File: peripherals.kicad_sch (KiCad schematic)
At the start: 15 parts, among them U5 LSM6DSO, U6 W25Q128JVS, U7 LIS3MDL

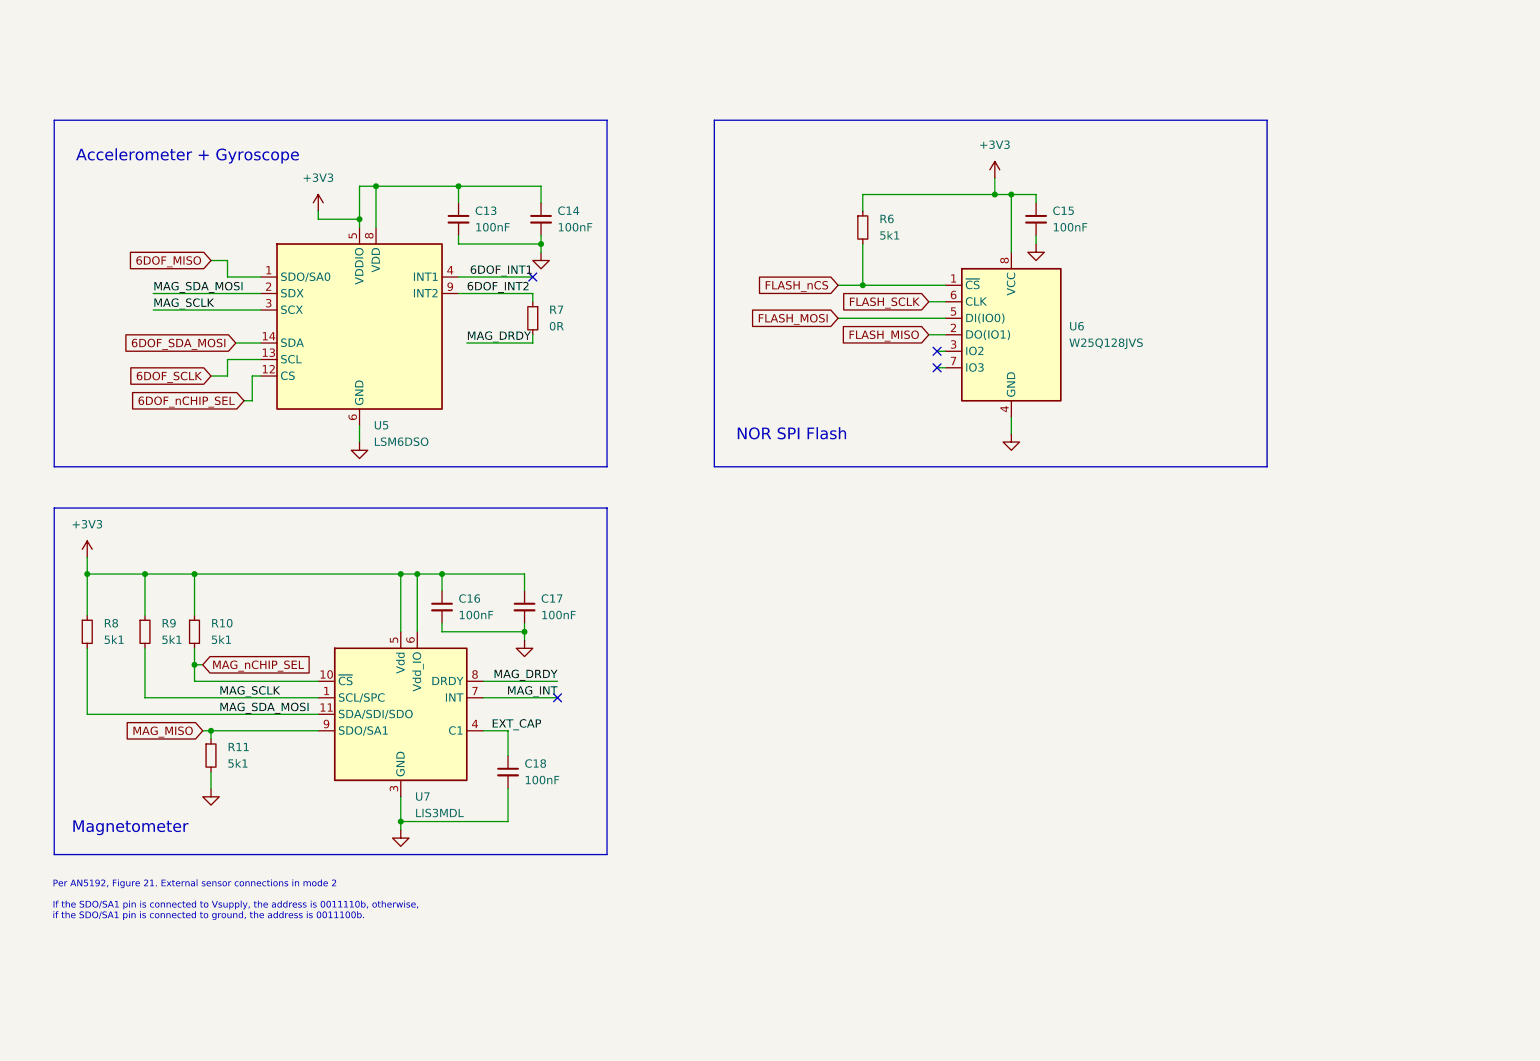
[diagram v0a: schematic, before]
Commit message: Added an I2C IO expander, plus 2 pushbuttons and  2 LEDs controlled by the expander
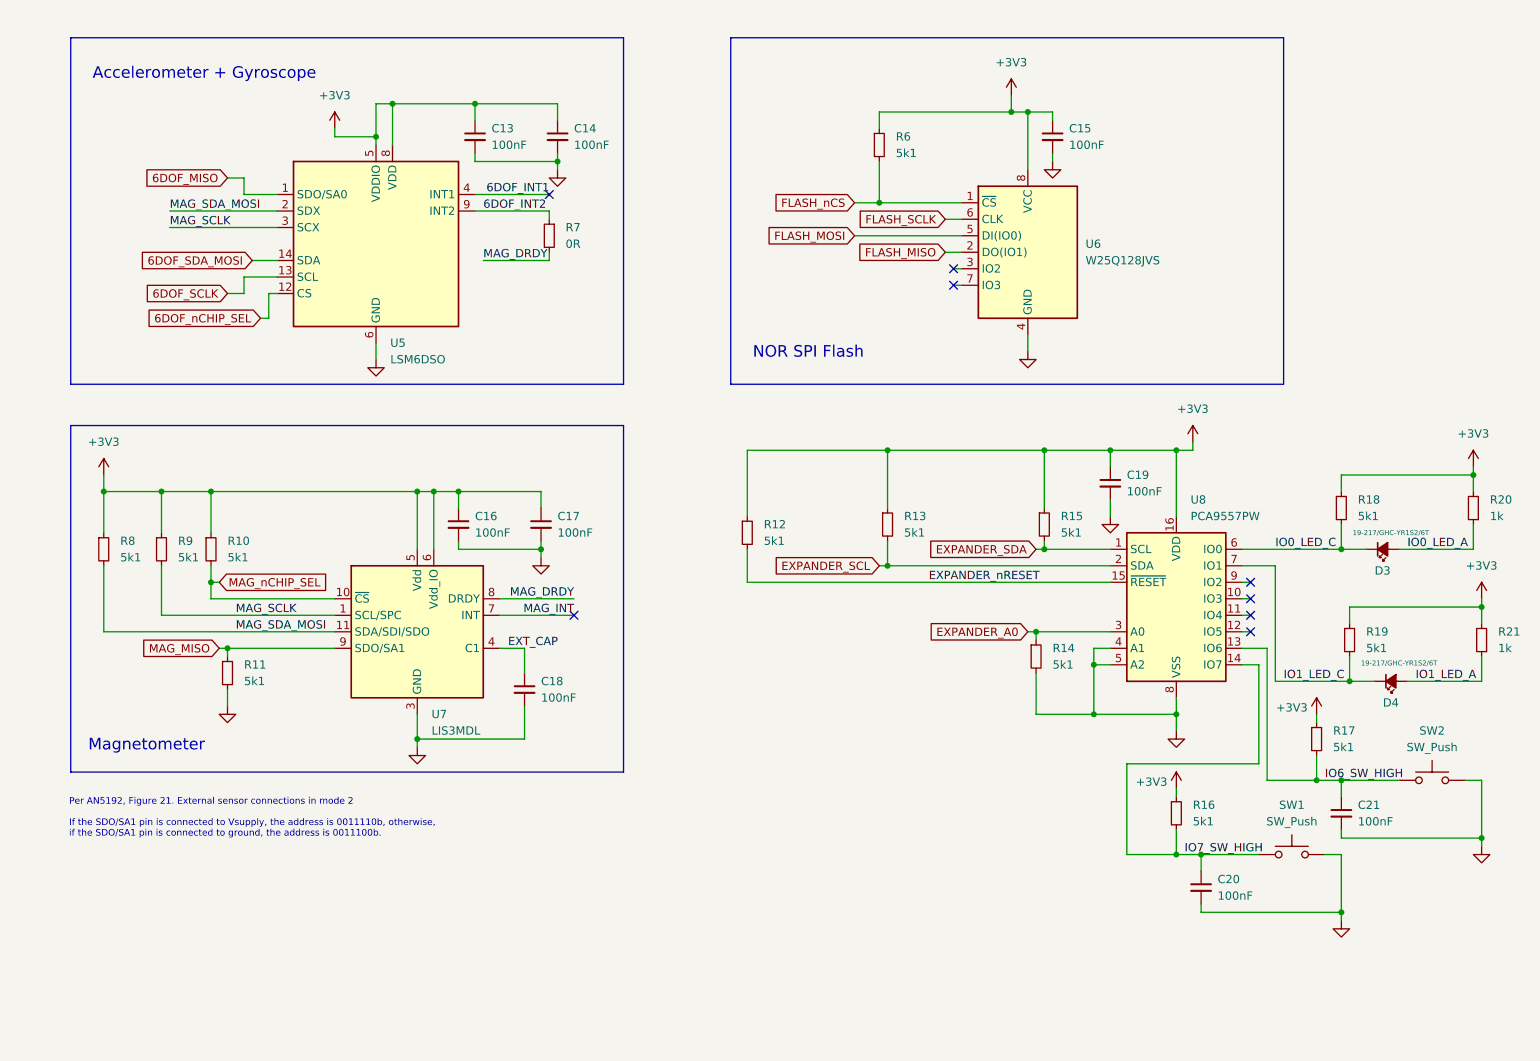
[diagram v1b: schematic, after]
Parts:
- added C19, C20, C21: 100nF, Capacitor_SMD:C_0402_1005Metric, symbol Device:C_Small
- added D3, D4: 19-217/GHC-YR1S2/6T, LED_SMD:LED_0603_1608Metric, symbol Device:LED_Small_Filled
- added R12, R13, R14, R15, R16, R17, R18, R19: 5k1, Resistor_SMD:R_0603_1608Metric, symbol Device:R_Small
- added R20, R21: 1k, Resistor_SMD:R_0603_1608Metric, symbol Device:R_Small
- added SW1, SW2: SW_Push, Button_Switch_SMD:SW_Push_1P1T_XKB_TS-1187A, symbol Switch:SW_Push
- added U8: PCA9557PW, Package_SO:TSSOP-16_4.4x5mm_P0.65mm, symbol Interface_Expansion:PCA9557PW
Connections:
- net +3V3: now also C19.1, R12.1, R13.1, R15.1, R16.1, R17.1, R18.1, R19.1, R20.2, R21.2, U8.16 (VDD)
- net GND: now also C19.2, C20.2, C21.2, R14.2, SW1.2, SW2.2, U8.4 (A1), U8.5 (A2), U8.8 (VSS)
- new net EXPANDER_A0: R14.1, U8.3 (A0)
- new net EXPANDER_SCL: R13.2, U8.2 (SDA)
- new net EXPANDER_SDA: R15.2, U8.1 (SCL)
- new net EXPANDER_nRESET: R12.2, U8.15 (~{RESET})
- new net IO0_LED_A: D3.2 (A), R20.1
- new net IO0_LED_C: D3.1 (K), R18.2, U8.6 (IO0)
- new net IO1_LED_A: D4.2 (A), R21.1
- new net IO1_LED_C: D4.1 (K), R19.2, U8.7 (IO1)
- new net IO6_SW_HIGH: C21.1, R17.2, SW2.1, U8.13 (IO6)
- new net IO7_SW_HIGH: C20.1, R16.2, SW1.1, U8.14 (IO7)
- no-connect marks 4 -> 8
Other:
- moved on the sheet: C13, C14, C15, C16, C17, C18, R10, R11, R6, R7, R8, R9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

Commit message: Cleaned up schematic with comments from datasheets.  Added stitching vias to PCB
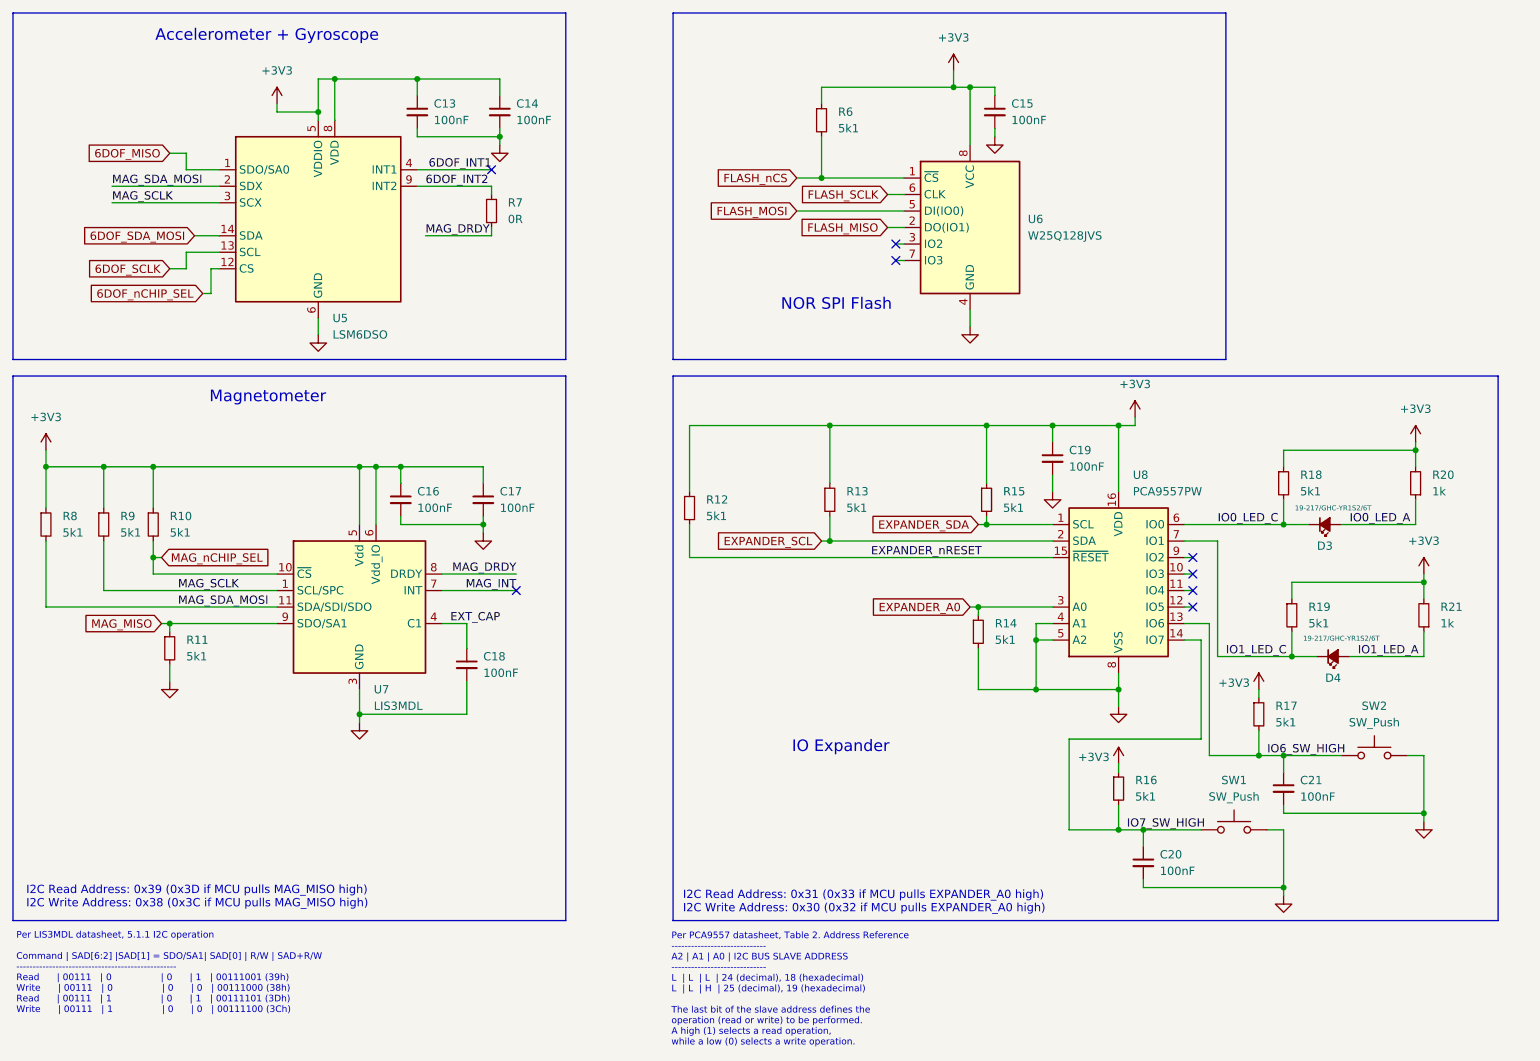
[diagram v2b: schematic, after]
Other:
- note added: "I2C Read Address: 0x31 (0x33 if MCU pulls EXPANDER_A0 high) I2C Write Address: 0x30 (0x32 if MCU pulls EXPANDER_A0 high)"
- note added: "I2C Read Address: 0x39 (0x3D if MCU pulls MAG_MISO high) I2C Write Address: 0x38 (0x3C if MCU pulls MAG_MISO high)"
- note added: "IO Expander"
- note added: "Per LIS3MDL datasheet, 5.1.1 I2C operation Command | SAD[6:2] |SAD[1] = SDO/SA1| SAD[0] | R/W | SAD+R/W ------------------------------------------------- Read | 00111 | 0 | 0 | 1 | 00111001 (39h) Write | 00111 | 0 | 0 | 0 | 00111000 (38h) Read | 00111 | 1 | 0 | 1 | 00111101 (3Dh) Write | 00111 | 1 | 0 | 0 | 00111100 (3Ch)"
- note added: "Per PCA9557 datasheet, Table 2. Address Reference ----------------------------- A2 | A1 | A0 | I2C BUS SLAVE ADDRESS ----------------------------- L | L | L | 24 (decimal), 18 (hexadecimal) L | L | H | 25 (decimal), 19 (hexadecimal) The last bit of the slave address defines the operation (read or write) to be performed. A high (1) selects a read operation, while a low (0) selects a write operatio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"
- note removed: "Per AN5192, Figure 21. External sensor connections in mode 2 If the SDO/SA1 pin is connected to Vsupply, the address is 0011110b, otherwise, if the SDO/SA1 pin is connected to ground, the address is 0011100b."
- moved on the sheet: C13, C14, C15, C16, C17, C18, C19, C20, C21, D3, D4, R10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

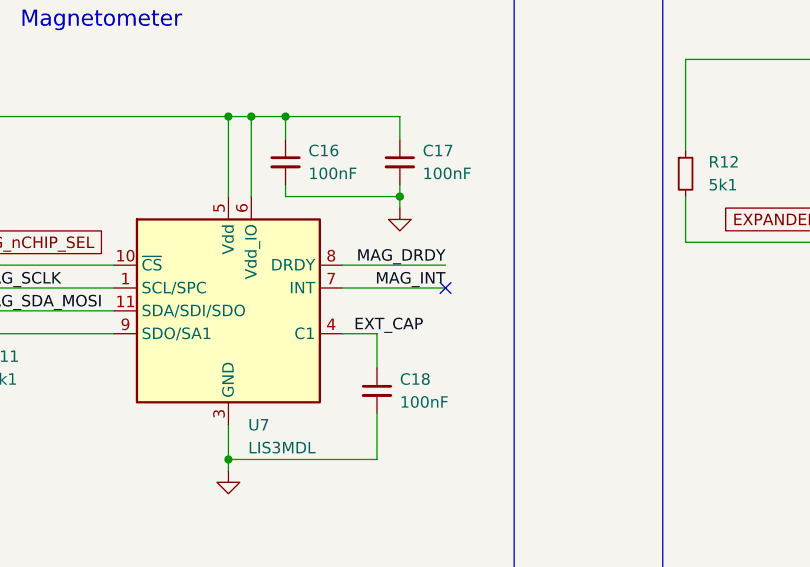
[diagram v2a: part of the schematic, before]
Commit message: Brought out INT pin from magnetometer to MCU, in case of need.  Updated layout accordingly
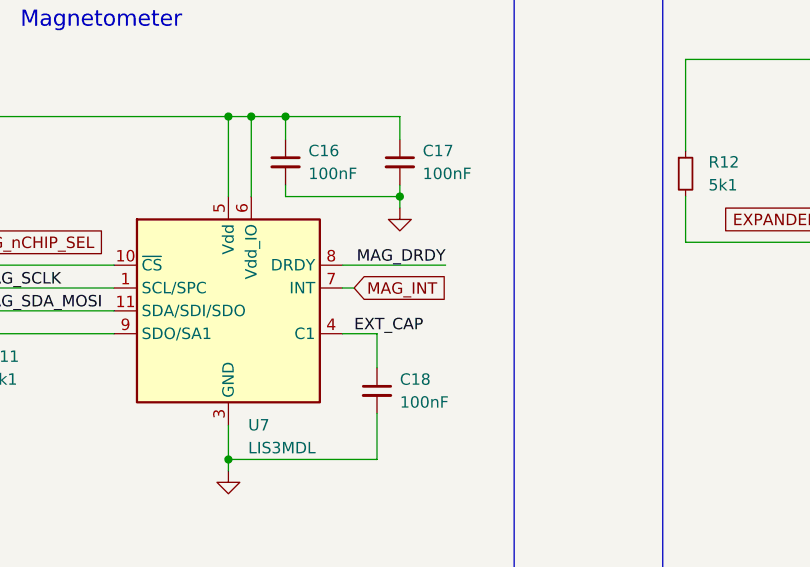
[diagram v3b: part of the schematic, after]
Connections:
- no-connect marks 8 -> 7
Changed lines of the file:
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@@
-	)
-	(no_connect
-		(at 111.76 111.76)
 	)
 	(no_connect
@@
 	(wire
 		(pts
-			(xy 100.33 111.76) (xy 111.76 111.76)
+			(xy 100.33 111.76) (xy 101.6 111.76)
 		)
 		(stroke
@@
 			)
 			(justify left bottom)
-		)
-	)
-	(label "MAG_INT"
-		(at 111.76 111.76 180)
-		(fields_autoplaced yes)
-		(effects
-			(font
-				(size 1.27 1.27)
-			)
-			(justify right bottom)
 		)
 	)
@@
 				(hide yes)
 			)
+		)
+	)
+	(global_label "MAG_INT"
+		(shape input)
+		(at 101.6 111.76 0)
+		(fields_autoplaced yes)
+		(effects
+			(font
+				(size 1.27 1.27)
+			)
+			(justify left)
+		)
+		(property "Intersheetrefs" "${INTERSHEET_REFS}"
+			(at 112.2657 111.76 0)
+			(effects
+				(font
+					(size 1.27 1.27)
+				)
+				(justify left)
+				(hide yes)
+			)

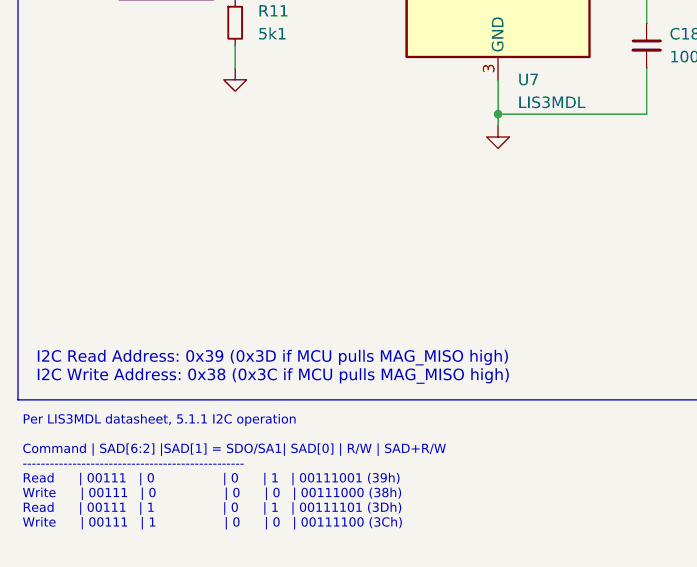
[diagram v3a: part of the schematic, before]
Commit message: Exported BOM, pick-and-place files.  Finalized schematic and exported PDF.  Files used to place JLCPCB order
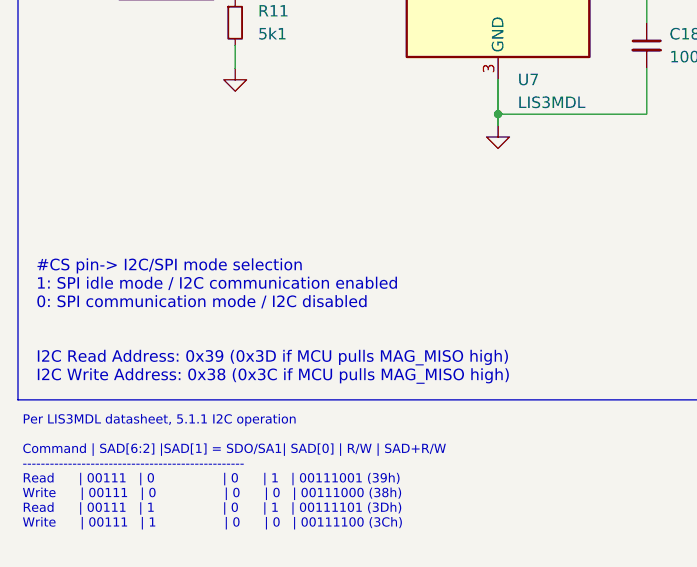
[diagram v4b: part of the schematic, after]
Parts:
- SW1, SW2: LCSC Part # (none) -> C318884; Manufacturer (none) -> XKB Connection
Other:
- note added: "#CS pin-> I2C/SPI mode selection 1: SPI idle mode / I2C communication enabled 0: SPI communication mode / I2C disabled"
